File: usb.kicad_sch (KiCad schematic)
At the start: 26 parts, among them J1 USB_C_Receptacle_USB2.0_14P, U1 SRV05-4, U2 CH334F, U3 M24C02-WMN, Y1 12Mhz

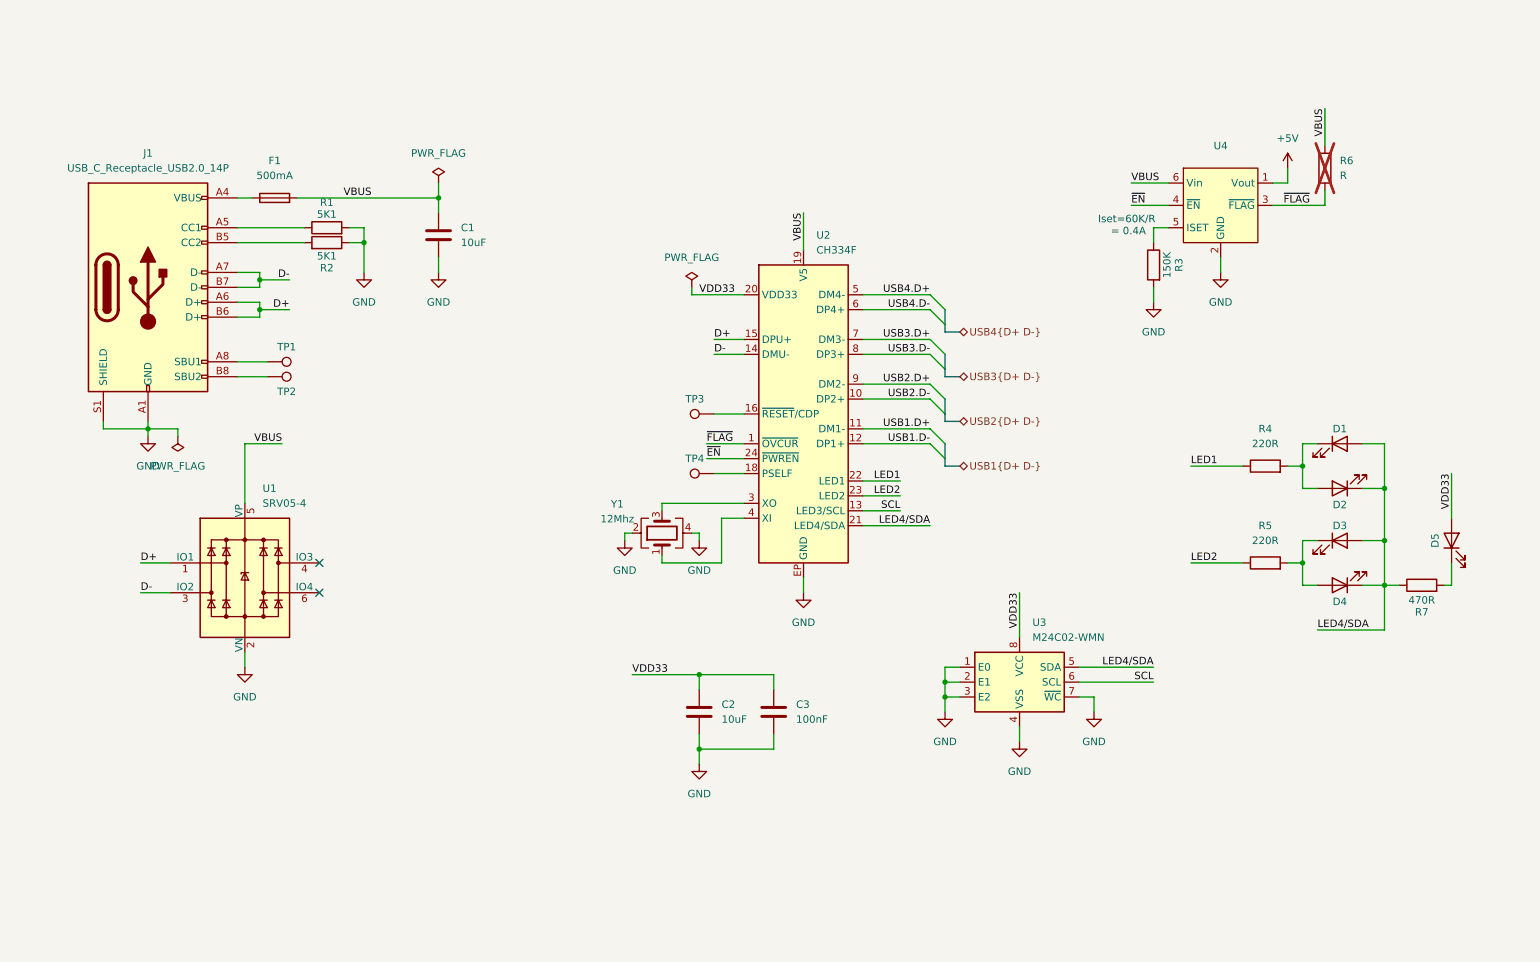
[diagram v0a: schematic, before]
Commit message: Add Uno shield
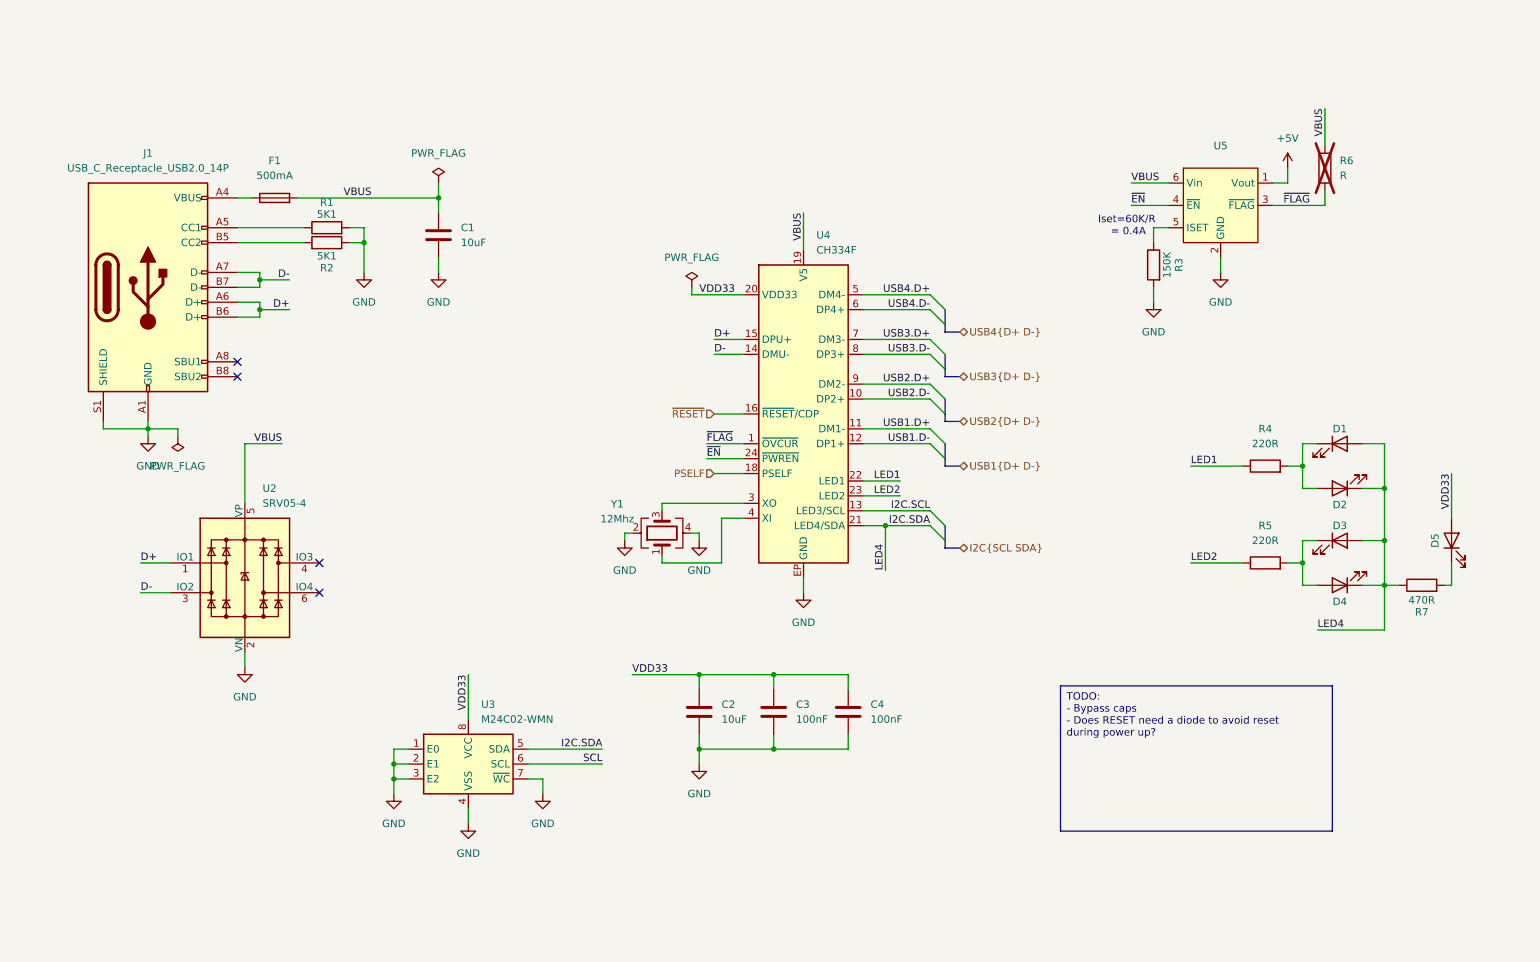
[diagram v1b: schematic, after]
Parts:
- removed TP1, TP2, TP3, TP4: TestPoint, TestPoint:TestPoint_Pad_D1.5mm, symbol Connector:TestPoint
- added C4: 100nF, Capacitor_SMD:C_0402_1005Metric, symbol Device:C
- renumbered U1 to U2, U2 to U4, U4 to U5
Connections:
- net GND: now also C4.2
- net SCL: no longer U4.13 (LED3/SCL)
- net VDD33: now also C4.1
- net ~{RESET}: now reaches U4.16 (~{RESET}/CDP)
- net PSELF: now reaches U4.18 (PSELF)
- net LED4/SDA renamed I2C.SDA
- new net I2C.SCL: U4.13 (LED3/SCL)
- no-connect marks 2 -> 4
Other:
- moved on the sheet: U3

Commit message: Add RP2350B from example
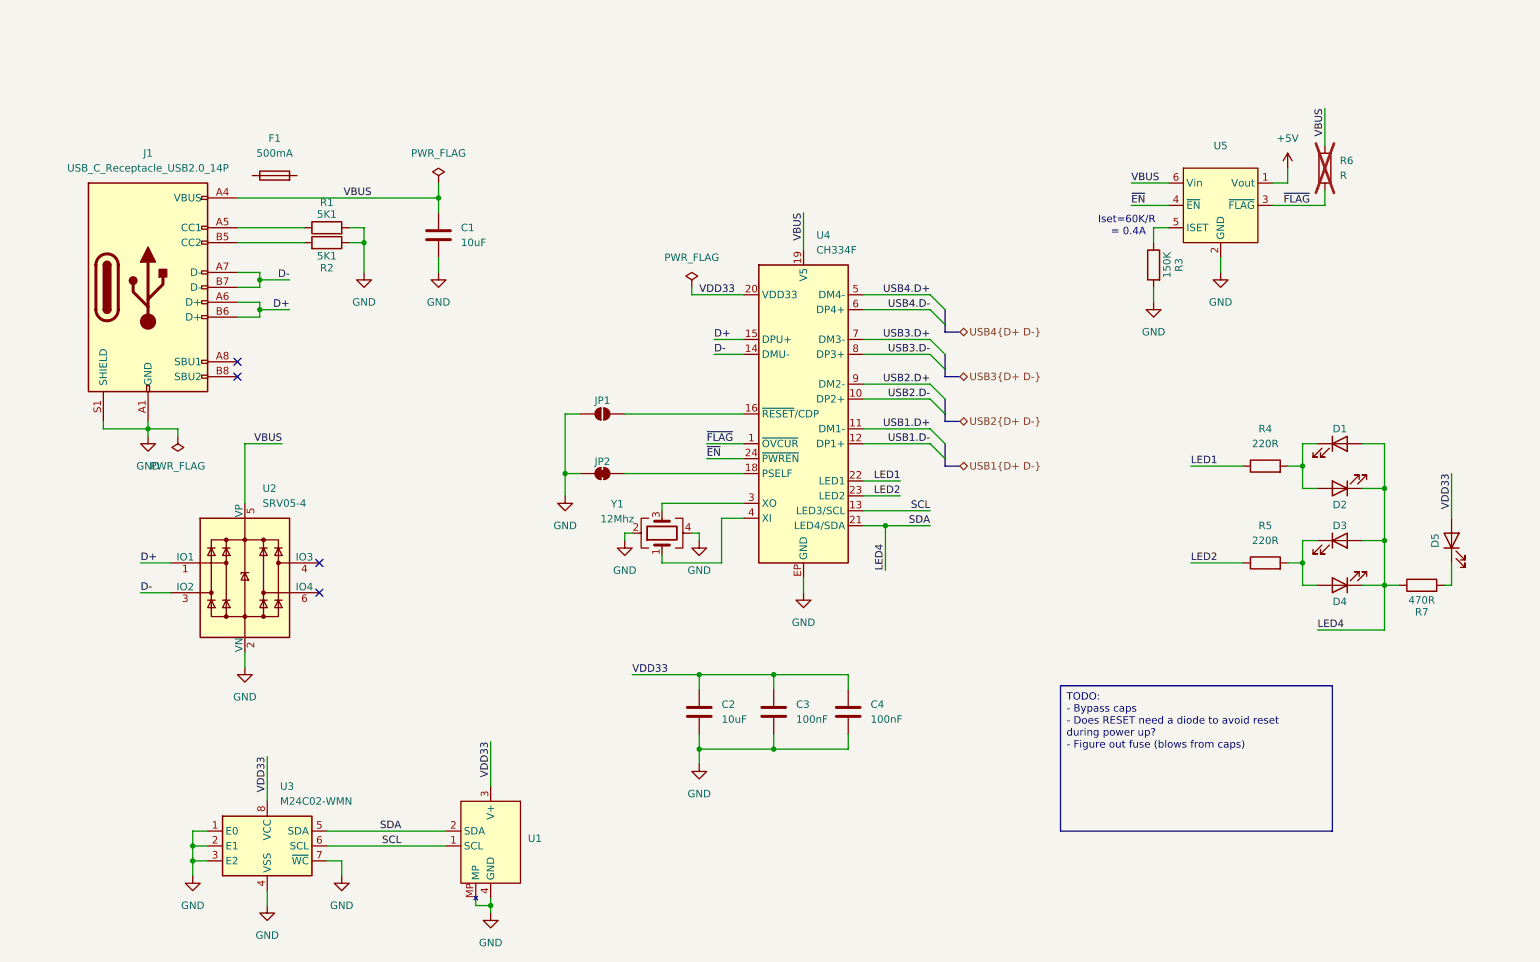
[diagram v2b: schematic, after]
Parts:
- added JP1: SolderJumper_2_Open, Jumper:SolderJumper-2_P1.3mm_Open_RoundedPad1.0x1.5mm, symbol Jumper:SolderJumper_2_Open
- added JP2: SolderJumper_2_Bridged, Jumper:SolderJumper-2_P1.3mm_Bridged_RoundedPad1.0x1.5mm, symbol Jumper:SolderJumper_2_Bridged
- added U1: ~, Connector_JST:JST_SH_SM04B-SRSS-TB_1x04-1MP_P1.00mm_Horizontal, symbol Project_Specific:StemmaQtTarget
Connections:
- net I2C.SCL is gone; now on net SCL: U4.13 (LED3/SCL)
- net GND: now also JP1.1 (A), JP2.1 (A), U1.4 (GND), U1.MP
- net SCL: now also U1.1 (SCL)
- net VBUS: now also J1.A4 (VBUS), J1.A9 (VBUS), J1.B4 (VBUS), J1.B9 (VBUS); no longer F1.2
- net VDD33: now also U1.3 (V+)
- net I2C.SDA renamed LED4
- net LED4: now also U1.2 (SDA)
- net PSELF: no longer names the net of U4.18 (PSELF)
- net PSELF: now also JP2.2 (B)
- net ~{RESET}: no longer names the net of U4.16 (~{RESET}/CDP)
- net ~{RESET}: now also JP1.2 (B)
- now unconnected: F1.1
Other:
- moved on the sheet: F1, U3

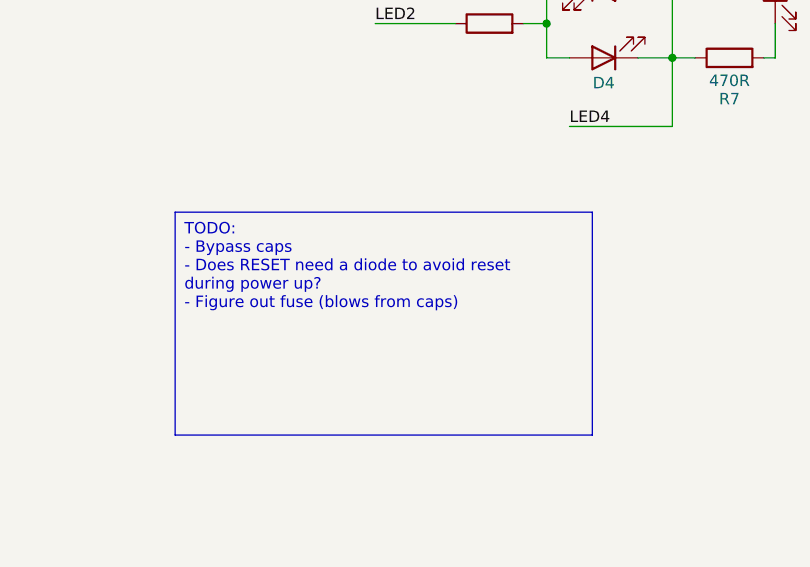
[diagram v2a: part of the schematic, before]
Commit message: Do pin assignment for tester
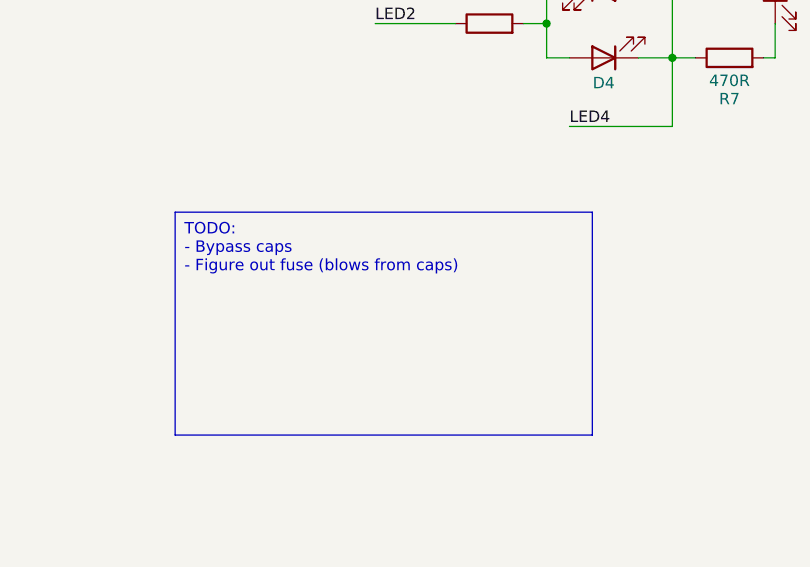
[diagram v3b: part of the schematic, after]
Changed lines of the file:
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@@
 		)
 	)
-	(text_box "TODO:\n- Bypass caps\n- Does RESET need a diode to avoid reset during power up?\n- Figure out fuse (blows from caps)"
+	(text_box "TODO:\n- Bypass caps\n- Figure out fuse (blows from caps)"
 		(exclude_from_sim no)
 		(at 196.215 130.175 0)

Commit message: Start Layout
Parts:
- removed F1: 500mA, Fuse:Fuse_1206_3216Metric_Pad1.42x1.75mm_HandSolder, symbol Device:Fuse
- added C12, C53, C54: 100uF, Capacitor_SMD:C_1206_3216Metric, symbol Device:C
- added C55: 1uF, Capacitor_SMD:C_0402_1005Metric, symbol Device:C
- added C56: 100nF, Capacitor_SMD:C_0402_1005Metric, symbol Device:C
- added C57: 22uF, Capacitor_SMD:C_0805_2012Metric, symbol Device:C
- added F2: 1A, Fuse:Fuse_1206_3216Metric_Pad1.42x1.75mm_HandSolder, symbol Device:Polyfuse
- added JP3, JP4, JP5: SolderJumper_2_Bridged, Jumper:SolderJumper-2_P1.3mm_Bridged_RoundedPad1.0x1.5mm, symbol Jumper:SolderJumper_2_Bridged
- added U15: AMS1117-3.3, Package_TO_SOT_SMD:SOT-223-3_TabPin2, symbol Regulator_Linear:AMS1117-3.3
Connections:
- net +5V: now also C12.1, C56.1, U15.3 (VI)
- net GND: now also C12.2, C53.2, C54.2, C55.2, C56.2, C57.2, U15.1 (GND)
- net LED4: now also JP4.1 (A); no longer U1.2 (SDA), U3.5 (SDA)
- net SCL: now also JP3.2 (B); no longer U4.13 (LED3/SCL)
- net VBUS: now also C53.1, C54.1, C55.1, F2.2; no longer J1.A4 (VBUS), J1.A9 (VBUS), J1.B4 (VBUS), J1.B9 (VBUS)
- net VDD33: now also JP5.2 (B); no longer U1.3 (V+), U3.8 (VCC)
- new net: JP5.1 (A), U1.3 (V+), U3.8 (VCC)
- new net: JP3.1 (A), U4.13 (LED3/SCL)
- new net: F2.1, J1.A4 (VBUS), J1.A9 (VBUS), J1.B4 (VBUS), J1.B9 (VBUS)
- new net +3V3: C57.1, U15.2 (VO)
- new net SDA: JP4.2 (B), U1.2 (SDA), U3.5 (SDA)
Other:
- moved on the sheet: C1, J1, R1, R2, R3, R6, U5

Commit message: Layout Tester and USB Hub
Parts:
- U4: footprint Package_DFN_QFN:QFN-24-1EP_4x4mm_P0.5mm_EP2.7x2.7mm -> Package_DFN_QFN:QFN-24-1EP_4x4mm_P0.5mm_EP2.7x2.7mm_ThermalVias
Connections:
- net D+: now also U2.3 (IO2), U2.4 (IO3); no longer U2.1 (IO1)
- net D-: now also U2.1 (IO1), U2.6 (IO4); no longer U2.3 (IO2)
- net GND: now also U4.25 (GND); no longer U4.EP (GND)
- net VDD33: no longer C4.1
- net at JP5.1 (A), U1.3 (V+), U3.8 (VCC): now also C4.1
- no-connect marks 4 -> 2
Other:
- moved on the sheet: C4
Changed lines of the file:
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@@
 	)
 	(junction
-		(at 147.32 140.97)
+		(at 34.29 64.77)
 		(diameter 0)
 		(color 0 0 0 0)
 	)
 	(junction
-		(at 34.29 64.77)
+		(at 71.12 33.02)
 		(diameter 0)
 		(color 0 0 0 0)
 	)
 	(junction
-		(at 71.12 33.02)
+		(at 60.96 140.97)
 		(diameter 0)
 		(color 0 0 0 0)
@@
 	)
 	(junction
-		(at 147.32 128.27)
-		(diameter 0)
-		(color 0 0 0 0)
-	)
-	(junction
 		(at 251.46 96.52)
 		(diameter 0)
@@
 		(at 49.53 53.34)
 	)
-	(no_connect
-		(at 69.85 114.3)
-	)
-	(no_connect
-		(at 69.85 109.22)
-	)
 	(bus_entry
 		(at 173.99 73.66)
@@
 	(wire
 		(pts
+			(xy 40.64 140.97) (xy 60.96 140.97)
+		)
+		(stroke
+			(width 0)
+			(type default)
+		)
+	)
+	(wire
+		(pts
 			(xy 99.06 140.97) (xy 60.96 140.97)
 		)
@@
 	(wire
 		(pts
-			(xy 44.45 114.3) (xy 39.37 114.3)
+			(xy 44.45 109.22) (xy 39.37 109.22)
 		)
 		(stroke
@@
 	(wire
 		(pts
-			(xy 44.45 109.22) (xy 39.37 109.22)
+			(xy 44.45 114.3) (xy 39.37 114.3)
 		)
 		(stroke
@@
 	(wire
 		(pts
+			(xy 40.64 151.13) (xy 40.64 153.67)
+		)
+		(stroke
+			(width 0)
+			(type default)
+		)
+	)
+	(wire
+		(pts
 			(xy 271.78 29.21) (xy 271.78 33.02)
 		)
@@
 	(wire
 		(pts
+			(xy 69.85 114.3) (xy 74.93 114.3)
+		)
+		(stroke
+			(width 0)
+			(type default)
+		)
+	)
+	(wire
+		(pts
 			(xy 162.56 71.12) (xy 173.99 71.12)
 		)
@@
 	(wire
 		(pts
-			(xy 160.02 128.27) (xy 147.32 128.27)
-		)
-		(stroke
-			(width 0)
-			(type default)
-		)
-	)
-	(wire
-		(pts
 			(xy 138.43 101.6) (xy 138.43 109.22)
 		)
@@
 	(wire
 		(pts
-			(xy 160.02 130.81) (xy 160.02 128.27)
+			(xy 68.58 33.02) (xy 71.12 33.02)
 		)
 		(stroke
@@
 	(wire
 		(pts
-			(xy 68.58 33.02) (xy 71.12 33.02)
+			(xy 73.66 160.02) (xy 73.66 162.56)
 		)
 		(stroke
@@
 	(wire
 		(pts
-			(xy 73.66 160.02) (xy 73.66 162.56)
+			(xy 49.53 33.02) (xy 60.96 33.02)
 		)
 		(stroke
@@
 	(wire
 		(pts
-			(xy 49.53 33.02) (xy 60.96 33.02)
+			(xy 251.46 105.41) (xy 251.46 113.03)
 		)
 		(stroke
@@
 	(wire
 		(pts
-			(xy 251.46 105.41) (xy 251.46 113.03)
+			(xy 34.29 63.5) (xy 34.29 64.77)
 		)
 		(stroke
@@
 	(wire
 		(pts
-			(xy 34.29 63.5) (xy 34.29 64.77)
+			(xy 152.4 111.76) (xy 152.4 114.3)
 		)
 		(stroke
@@
 	(wire
 		(pts
-			(xy 152.4 111.76) (xy 152.4 114.3)
+			(xy 247.65 105.41) (xy 251.46 105.41)
 		)
 		(stroke
@@
 	(wire
 		(pts
-			(xy 247.65 105.41) (xy 251.46 105.41)
+			(xy 40.64 140.97) (xy 40.64 143.51)
 		)
 		(stroke
@@
 	(wire
 		(pts
+			(xy 69.85 109.22) (xy 74.93 109.22)
+		)
+		(stroke
+			(width 0)
+			(type default)
+		)
+	)
+	(wire
+		(pts
 			(xy 134.62 128.27) (xy 134.62 130.81)
 		)
@@
 	(wire
 		(pts
-			(xy 160.02 138.43) (xy 160.02 140.97)
-		)
-		(stroke
-			(width 0)
-			(type default)
-		)
-	)
-	(wire
-		(pts
 			(xy 241.3 33.02) (xy 236.22 33.02)
 		)
@@
 	(wire
 		(pts
-			(xy 160.02 140.97) (xy 147.32 140.97)
-		)
-		(stroke
-			(width 0)
-			(type default)
-		)
-	)
-	(wire
-		(pts
 			(xy 162.56 95.25) (xy 168.91 95.25)
 		)
@@
 		)
 	)
+	(label "D-"
+		(at 74.93 114.3 180)
+		(effects
+			(font
+				(size 1.27 1.27)
+			)
+			(justify right bottom)
+		)
+	)
 	(label "~{FLAG}"
 		(at 135.89 88.9 0)
@@
 	)
 	(label "D+"
-		(at 39.37 109.22 0)
+		(at 39.37 114.3 0)
 		(effects
 			(font
@@
 		)
 	)
+	(label "D+"
+		(at 74.93 109.22 180)
+		(effects
+			(font
+				(size 1.27 1.27)
+			)
+			(justify right bottom)
+		)
+	)
 	(label "VDD33"
 		(at 262.89 93.98 270)
@@
 	)
 	(label "D-"
-		(at 39.37 114.3 0)
+		(at 39.37 109.22 0)
 		(effects
 			(font
@@
 			)
 		)
-		(property "Footprint" "Package_DFN_QFN:QFN-24-1EP_4x4mm_P0.5mm_EP2.7x2.7mm"
+		(property "Footprint" "Package_DFN_QFN:QFN-24-1EP_4x4mm_P0.5mm_EP2.7x2.7mm_ThermalVias"
 			(at 155.956 116.586 0)
 			(effects
@@
 		(pin "21"
 		)
-		(pin "EP"
+		(pin "25"
 		)
 		(pin "20"
@@
 	)
 	(symbol
+		(lib_id "power:GND")
+		(at 40.64 153.67 0)
+		(unit 1)
+		(exclude_from_sim no)
+		(in_bom yes)
+		(on_board yes)
+		(dnp no)
+		(fields_autoplaced yes)
+		(property "Reference" "#PWR0102"
+			(at 40.64 160.02 0)
+			(effects
+				(font
+					(size 1.27 1.27)
+				)
+				(hide yes)
+			)
+		)
+		(property "Value" "GND"
+			(at 40.64 158.75 0)
+			(effects
+				(font
+					(size 1.27 1.27)
+				)
+			)
+		)
+		(property "Footprint" ""
+			(at 40.64 153.67 0)
+			(effects
+				(font
+					(size 1.27 1.27)
+				)
+				(hide yes)
+			)
+		)
+		(property "Datasheet" ""
+			(at 40.64 153.67 0)
+			(effects
+				(font
+					(size 1.27 1.27)
+				)
+				(hide yes)
+			)
+		)
+		(property "Description" "Power symbol creates a global label with name \"GND\" , ground"
+			(at 40.64 153.67 0)
+			(effects
+				(font
+					(size 1.27 1.27)
+				)
+				(hide yes)
+			)
+		)
+		(pin "1"
+		)
+		(instances
+			(project "shield"
+				(path "/d57ea000-ef46-42c0-b86a-7e6b1d4431c2/b15cbb63-0434-4f0a-85e4-7f3e94e11f27"
+					(reference "#PWR0102")
+					(unit 1)
+				)
+			)
+		)
+	)
+	(symbol
 		(lib_id "Device:C")
 		(at 109.22 31.75 0)
@@
 	(symbol
 		(lib_id "Device:C")
-		(at 160.02 134.62 0)
+		(at 40.64 147.32 0)
+		(mirror y)
 		(unit 1)
 		(exclude_from_sim no)
@@
 		(fields_autoplaced yes)
 		(property "Reference" "C4"
-			(at 163.83 133.3499 0)
+			(at 36.83 146.0499 0)
 			(effects
 				(font
@@
 		)
 		(property "Value" "100nF"
-			(at 163.83 135.8899 0)
+			(at 36.83 148.5899 0)
 			(effects
 				(font
@@
 		)
 		(property "Footprint" "Capacitor_SMD:C_0402_1005Metric"
-			(at 160.9852 138.43 0)
+			(at 39.6748 151.13 0)
 			(effects
 				(font
@@
 		)
 		(property "Datasheet" "~"
-			(at 160.02 134.62 0)
+			(at 40.64 147.32 0)
 			(effects
 				(font
@@
 		)
 		(property "Description" "Unpolarized capacitor"
-			(at 160.02 134.62 0)
+			(at 40.64 147.32 0)
 			(effects
 				(font
@@
 		)
 		(property "LCSC" "C1525"
-			(at 160.02 134.62 0)
+			(at 40.64 147.32 0)
 			(effects
 				(font

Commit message: WIP
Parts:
- U3: LCSC (none) -> C7562
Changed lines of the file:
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@@
+			)
+		)
+		(property "LCSC" "C7562"
+			(at 60.96 157.48 0)
+			(effects
+				(font
+					(size 1.27 1.27)
+				)
+				(hide yes)
 			)
 		)

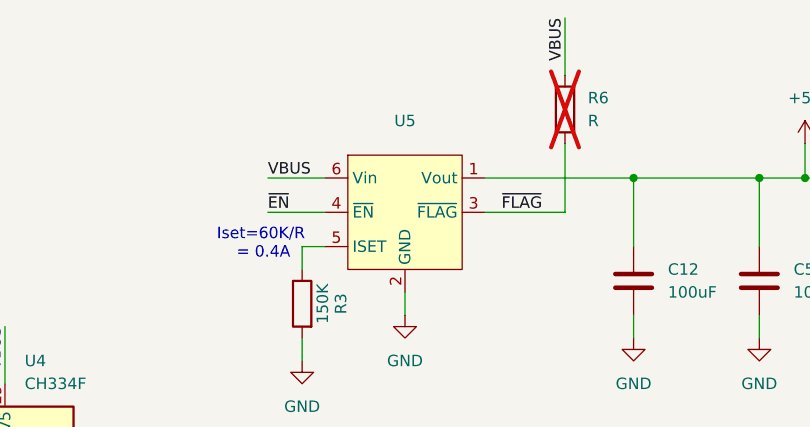
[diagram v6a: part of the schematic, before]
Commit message: JLC rotations
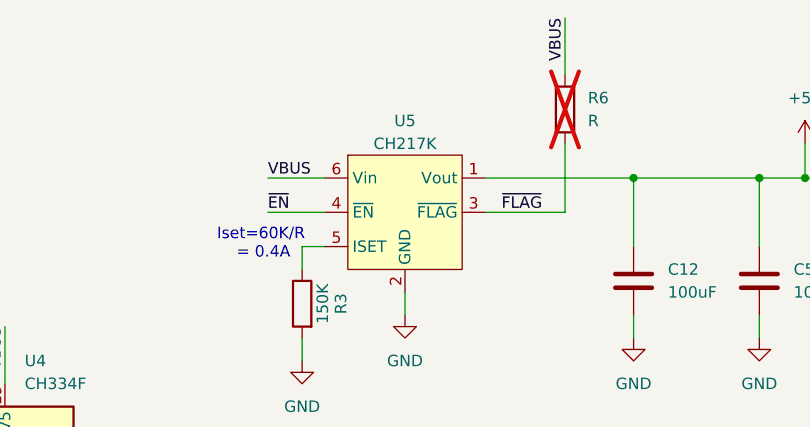
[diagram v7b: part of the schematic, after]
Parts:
- U2: FT Rotation Offset (none) -> 90
- U4: FT Rotation Offset (none) -> 180
- U5: value ~ -> CH217K; FT Rotation Offset (none) -> 90
